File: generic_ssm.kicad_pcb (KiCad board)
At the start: 4 copper layers, 80 x 80 mm, 20 parts, among them J1 RST_JMP, J2 DEBUG CONN, J3 PROGRAMMING PORT, SW1 SW_RST, U1 SN65HVD233, U2 ATMEGA32M1-MU, Y1 8MHz

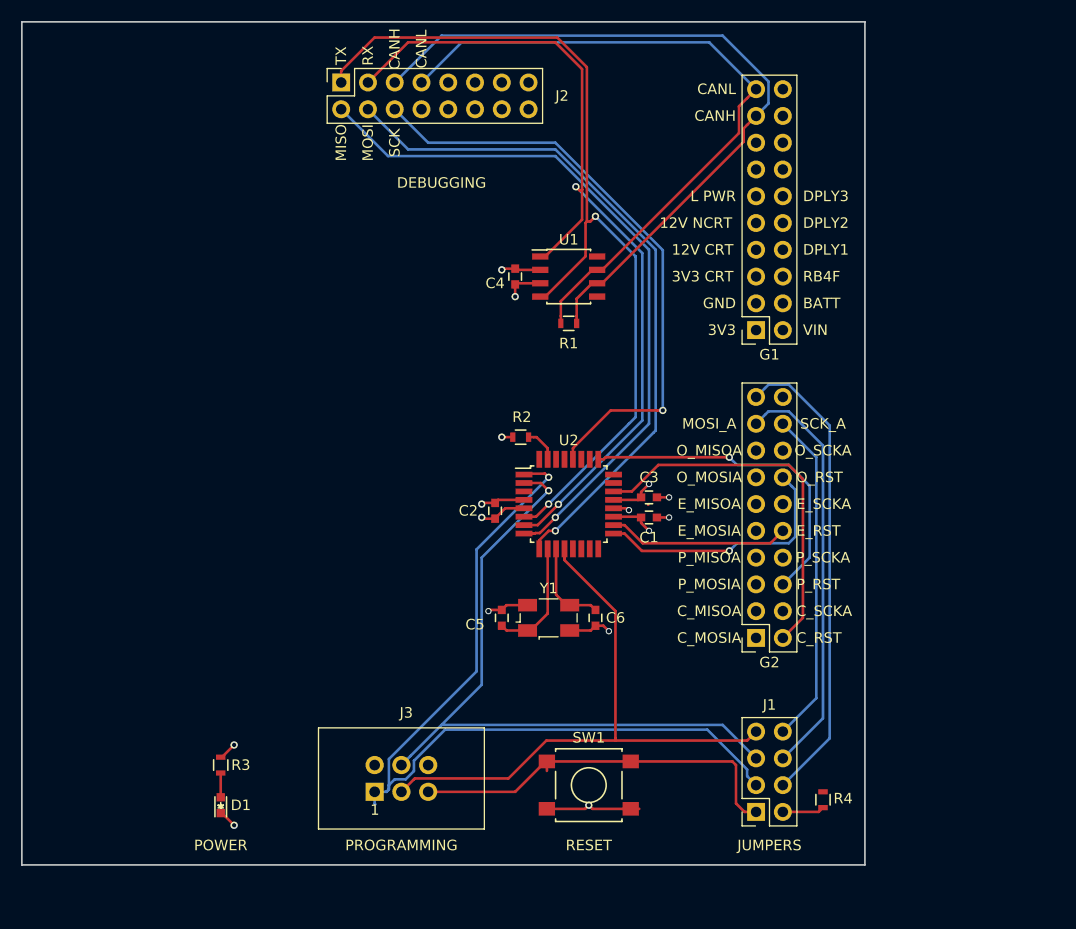
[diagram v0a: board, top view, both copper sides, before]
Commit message: Ease-of-use changes to PCB routing.
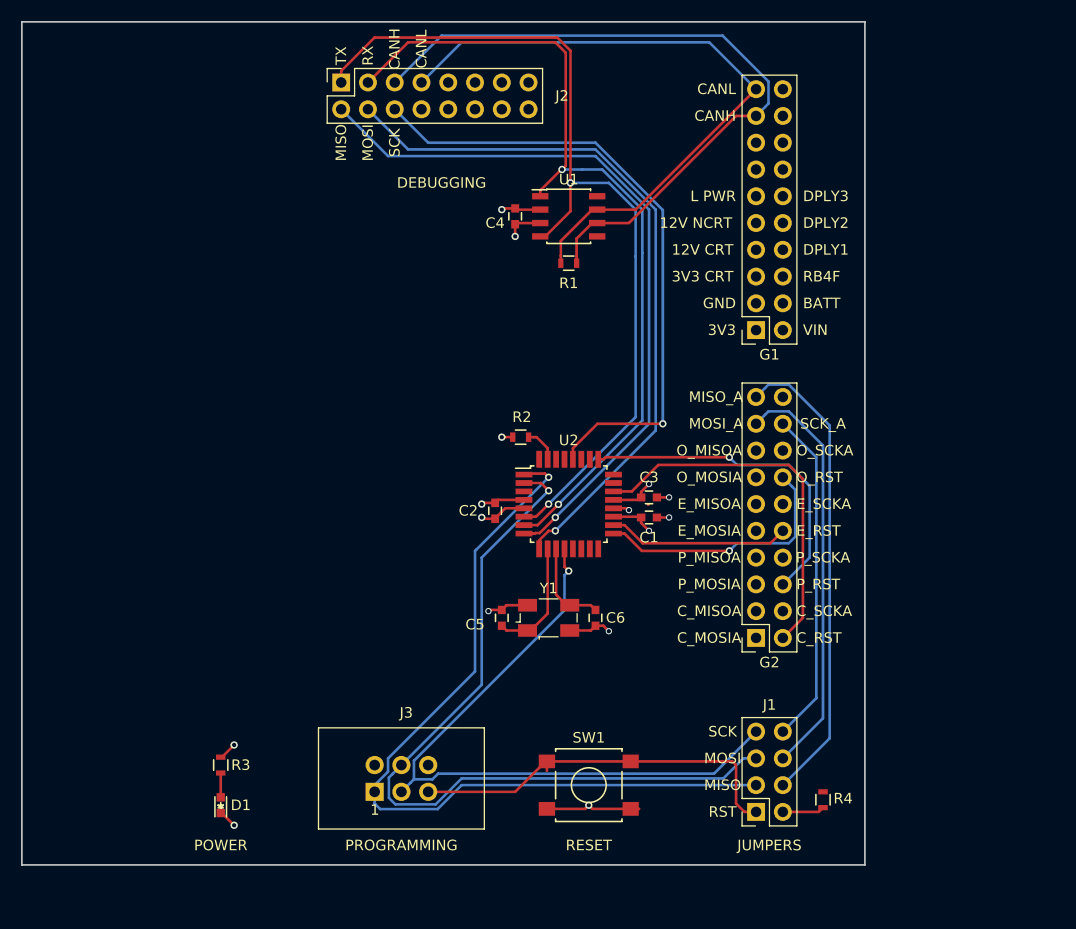
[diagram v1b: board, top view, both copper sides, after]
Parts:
- moved C4 5.72 mm to (146.8, 68.5)
- moved R1 5.72 mm to (151.9, 72.9)
- moved U1 5.72 mm to (151.9, 68.5)
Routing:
- net /MOSI_A: track 65.8 -> 75.1 mm
- net /SCK_A: track 57.3 -> 64.1 mm, vias 0 -> 1
- net /MISO_A: track 81.7 -> 77.8 mm
- net /CANL: track 65.6 -> 62.2 mm
- net /RX_CAN: track 83.6 -> 80.4 mm
- net /SCK: track 57.3 -> 60.2 mm
- net /CANH: track 70.2 -> 67.5 mm
- net /MOSI: track 66.2 -> 68.4 mm
- net /MISO: track 68.2 -> 70.5 mm
- net /TX_CAN: track 86.9 -> 85.2 mm
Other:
- board text added: "MISO_A"
- board text added: "RST"

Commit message: Minor Changes
Fixed via sizes, fixed resistors on schematic
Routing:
- net /SCK: track 60.2 -> 61.2 mm
- net GND: track 30.9 -> 31.5 mm
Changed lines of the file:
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@@
     (links 64)
     (no_connects 19)
-    (area 99.924999 49.924999 180.075001 130.075001)
+    (area 99.924999 46.723 218.11224 130.075001)
     (thickness 1.6)
     (drawings 56)
-    (tracks 271)
+    (tracks 280)
     (zones 0)
     (modules 20)
@@
     (aux_axis_origin 0 0)
     (grid_origin 12.192 12.573)
-    (visible_elements FFFEFF7F)
+    (visible_elements 7FFFFFFF)
     (pcbplotparams
       (layerselection 0x00030_80000001)
@@
   (gr_line (start 100 50) (end 180 50) (angle 90) (layer Edge.Cuts) (width 0.15))
   (segment (start 159.422001 95.823001) (end 159.487001 95.758001) (width 0.25) (layer F.Cu) (net 0))
+  (segment (start 157.5862 96.3122) (end 157.7894 96.3122) (width 0.25) (layer F.Cu) (net 1))
+  (via (at 157.861 96.2406) (size 0.7) (drill 0.4) (layers F.Cu B.Cu) (net 1))
+  (segment (start 157.7894 96.3122) (end 157.861 96.2406) (width 0.25) (layer F.Cu) (net 1))
+  (via (at 155.702 107.823) (size 0.7) (drill 0.4) (layers F.Cu B.Cu) (net 1))
+  (segment (start 144.272 105.918) (end 144.387 105.803) (width 0.25) (layer F.Cu) (net 1))
+  (segment (start 144.387 105.803) (end 144.272 105.918) (width 0.25) (layer F.Cu) (net 1))
+  (via (at 144.387 105.803) (size 0.7) (drill 0.4) (layers F.Cu B.Cu) (net 1))
+  (segment (start 144.387 105.803) (end 144.3736 105.8164) (width 0.25) (layer B.Cu) (net 1))
+  (segment (start 144.3736 105.8164) (end 144.3228 105.8164) (width 0.25) (layer B.Cu) (net 1))
   (segment (start 149.822 124.678) (end 153.452 124.678) (width 0.25) (layer F.Cu) (net 1))
   (segment (start 153.452 124.678) (end 153.797 124.333) (width 0.25) (layer F.Cu) (net 1))
@@
   (segment (start 157.772 124.678) (end 158.587 124.678) (width 0.25) (layer F.Cu) (net 1))
   (segment (start 156.142 96.158) (end 157.432 96.158) (width 0.25) (layer F.Cu) (net 1))
-  (via (at 157.607 96.333) (size 0.6) (drill 0.4) (layers F.Cu B.Cu) (net 1))
-  (segment (start 157.432 96.158) (end 157.607 96.333) (width 0.25) (layer F.Cu) (net 1))
+  (segment (start 157.432 96.158) (end 157.5862 96.3122) (width 0.25) (layer F.Cu) (net 1))
+  (segment (start 157.5862 96.3122) (end 157.607 96.333) (width 0.25) (layer F.Cu) (net 1))
   (segment (start 160.262 97.028) (end 161.417 97.028) (width 0.25) (layer F.Cu) (net 1))
-  (via (at 161.417 97.028) (size 0.6) (drill 0.4) (layers F.Cu B.Cu) (net 1))
+  (via (at 161.417 97.028) (size 0.7) (drill 0.4) (layers F.Cu B.Cu) (net 1))
   (segment (start 160.262 95.123) (end 161.417 95.123) (width 0.25) (layer F.Cu) (net 1))
-  (via (at 161.417 95.123) (size 0.6) (drill 0.4) (layers F.Cu B.Cu) (net 1))
+  (via (at 161.417 95.123) (size 0.7) (drill 0.4) (layers F.Cu B.Cu) (net 1))
   (segment (start 145.542 105.803) (end 144.387 105.803) (width 0.25) (layer F.Cu) (net 1))
-  (segment (start 144.387 105.803) (end 144.272 105.918) (width 0.25) (layer F.Cu) (net 1))
-  (via (at 144.272 105.918) (size 0.6) (drill 0.4) (layers F.Cu B.Cu) (net 1))
   (segment (start 147.987 105.353) (end 145.992 105.353) (width 0.25) (layer F.Cu) (net 1))
   (segment (start 145.992 105.353) (end 145.542 105.803) (width 0.25) (layer F.Cu) (net 1))
   (segment (start 154.432 107.303) (end 155.182 107.303) (width 0.25) (layer F.Cu) (net 1))
   (segment (start 155.182 107.303) (end 155.702 107.823) (width 0.25) (layer F.Cu) (net 1))
-  (via (at 155.702 107.823) (size 0.6) (drill 0.4) (layers F.Cu B.Cu) (net 1))
   (segment (start 151.987 107.753) (end 153.982 107.753) (width 0.25) (layer F.Cu) (net 1))
   (segment (start 153.982 107.753) (end 154.432 107.303) (width 0.25) (layer F.Cu) (net 1))
+  (segment (start 159.4993 93.8657) (end 159.8041 93.8657) (width 0.25) (layer F.Cu) (net 2))
+  (via (at 159.893 93.7768) (size 0.7) (drill 0.4) (layers F.Cu B.Cu) (net 2))
+  (segment (start 159.8041 93.8657) (end 159.893 93.7768) (width 0.25) (layer F.Cu) (net 2))
   (segment (start 146.582 89.408) (end 145.542 89.408) (width 0.25) (layer F.Cu) (net 2))
   (via (at 145.542 89.408) (size 0.7) (drill 0.4) (layers F.Cu B.Cu) (net 2))
@@
   (via (at 120.142 118.618) (size 0.7) (drill 0.4) (layers F.Cu B.Cu) (net 2))
   (segment (start 158.762 95.123) (end 158.762 94.603) (width 0.25) (layer F.Cu) (net 2))
-  (segment (start 158.762 94.603) (end 159.512 93.853) (width 0.25) (layer F.Cu) (net 2))
-  (via (at 159.512 93.853) (size 0.6) (drill 0.4) (layers F.Cu B.Cu) (net 2))
+  (segment (start 158.762 94.603) (end 159.4993 93.8657) (width 0.25) (layer F.Cu) (net 2))
+  (segment (start 159.4993 93.8657) (end 159.512 93.853) (width 0.25) (layer F.Cu) (net 2))
   (segment (start 156.142 95.358) (end 158.527 95.358) (width 0.25) (layer F.Cu) (net 2))
   (segment (start 158.527 95.358) (end 158.762 95.123) (width 0.25) (layer F.Cu) (net 2))
   (segment (start 158.762 97.028) (end 158.762 97.548) (width 0.25) (layer F.Cu) (net 2))
   (segment (start 158.762 97.548) (end 159.512 98.298) (width 0.25) (layer F.Cu) (net 2))
-  (via (at 159.512 98.298) (size 0.6) (drill 0.4) (layers F.Cu B.Cu) (net 2))
+  (via (at 159.512 98.298) (size 0.7) (drill 0.4) (layers F.Cu B.Cu) (net 2))
   (segment (start 156.142 96.958) (end 158.692 96.958) (width 0.25) (layer F.Cu) (net 2))
   (segment (start 158.692 96.958) (end 158.762 97.028) (width 0.25) (layer F.Cu) (net 2))
@@
   (segment (start 149.9926 98.298) (end 150.622 98.298) (width 0.25) (layer F.Cu) (net 49))
   (via (at 150.622 98.298) (size 0.7) (drill 0.4) (layers F.Cu B.Cu) (net 49))
-  (segment (start 160.822 88.138) (end 160.822 67.85518) (width 0.25) (layer B.Cu) (net 50))
-  (segment (start 160.822 67.85518) (end 154.43482 61.468) (width 0.25) (layer B.Cu) (net 50))
+  (segment (start 161.3916 88.138) (end 161.4424 67.8688) (width 0.25) (layer B.Cu) (net 50))
+  (segment (start 161.4424 67.8688) (end 154.43482 61.468) (width 0.25) (layer B.Cu) (net 50))
   (segment (start 154.43482 61.468) (end 138.557 61.468) (width 0.25) (layer B.Cu) (net 50))
   (segment (start 138.557 61.468) (end 135.382 58.293) (width 0.25) (layer B.Cu) (net 50))
   (segment (start 152.292 91.508) (end 152.292 90.458) (width 0.25) (layer F.Cu) (net 50))
   (segment (start 152.292 90.458) (end 154.612 88.138) (width 0.25) (layer F.Cu) (net 50))
-  (segment (start 154.612 88.138) (end 160.822 88.138) (width 0.25) (layer F.Cu) (net 50))
-  (via (at 160.822 88.138) (size 0.7) (drill 0.4) (layers F.Cu B.Cu) (net 50))
+  (segment (start 154.612 88.138) (end 161.3916 88.138) (width 0.25) (layer F.Cu) (net 50))
+  (via (at 161.3916 88.138) (size 0.7) (drill 0.4) (layers F.Cu B.Cu) (net 50))
   (segment (start 154.592 69.088) (end 157.60841 69.088) (width 0.25) (layer F.Cu) (net 60))
   (segment (start 157.60841 69.088) (end 167.76841 58.928) (width 0.25) (layer F.Cu) (net 60))

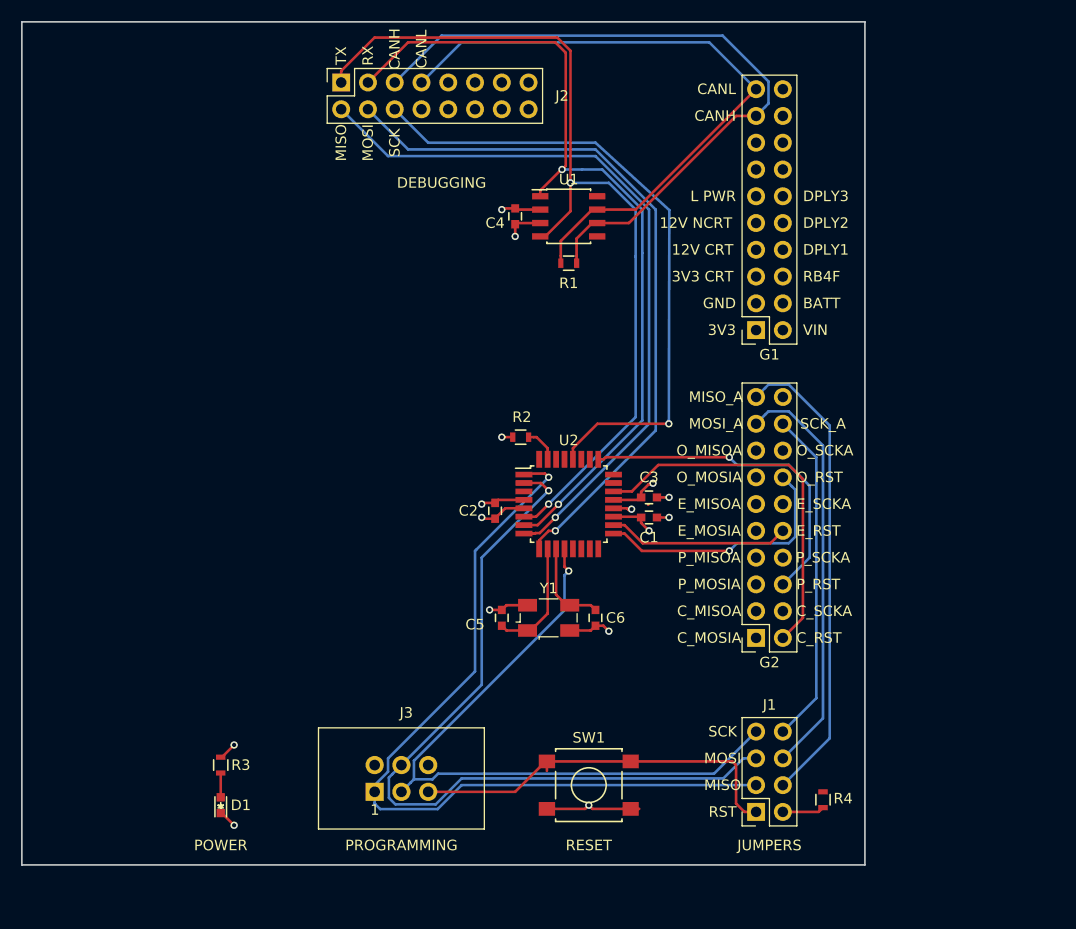
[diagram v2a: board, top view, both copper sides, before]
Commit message: Remade PCB layout for different header positions.
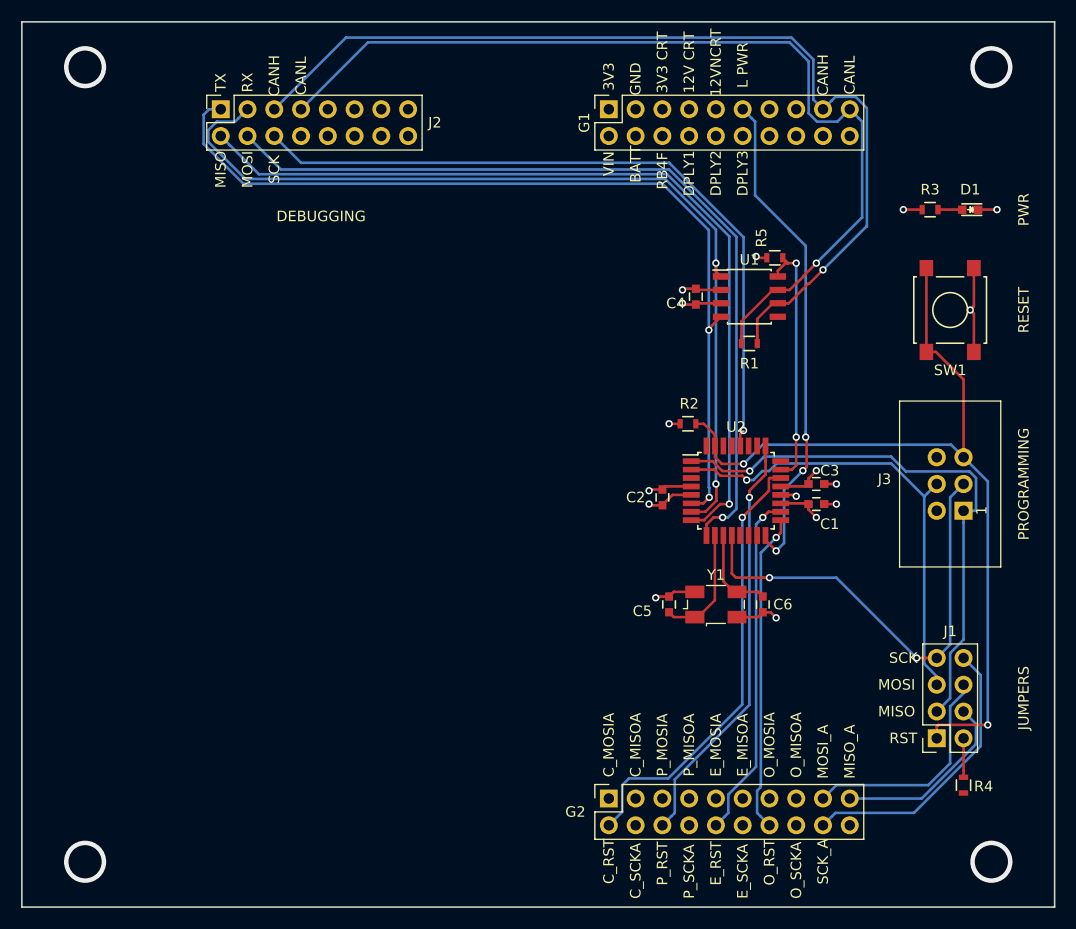
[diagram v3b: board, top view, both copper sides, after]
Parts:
- added R5: 1K, Resistors_SMD:R_0603, F.Cu at (171.4, 72.4)
- R2: value 120R -> 10K
- R4: value 10R -> 120R
- U1: value SN65HVD233 -> SN65HVD230
- moved D1 90.8 mm to (190.0, 67.8), turned to 180 degrees
- moved R3 85.5 mm to (186.2, 67.8), turned to 0 degrees
- moved J3 61.9 mm to (189.4, 96.4), turned to 90 degrees
- moved SW1 56.6 mm to (188.1, 77.3), turned to 90 degrees
- moved G1 25.2 mm to (155.7, 58.3), turned to 90 degrees
- moved G2 20.7 mm to (155.7, 123.7), turned to 90 degrees
- moved R1 18.8 mm to (169.0, 80.5)
- moved U1 18.8 mm to (169.0, 76.1)
- moved C4 18.8 mm to (164.0, 76.1)
- moved J1 18.5 mm to (186.8, 118.0)
- moved C1 15.9 mm to (175.4, 95.8)
- moved C2 15.9 mm to (160.8, 95.1)
- moved C3 15.9 mm to (175.4, 93.9)
- moved C5 15.9 mm to (161.4, 105.3)
- moved C6 15.9 mm to (170.3, 105.3)
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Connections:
- U1 pad 8: GND -> /CAN_LPWR
- U2 pad 16: Net-(U2-Pad16) -> /LOPWR
- U2 pad 23: Net-(U2-Pad23) -> /CAN_LPWR
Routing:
- net /LOPWR: track 0.00 -> 48.0 mm, vias 0 -> 3
- net /RST: track 40.7 -> 81.7 mm, vias 0 -> 2
- net /MOSI_A: track 75.1 -> 44.5 mm
- net /CANL: track 62.2 -> 90.1 mm, vias 0 -> 1
- net /MISO_A_COMMON: track 45.0 -> 18.5 mm
- net /CANH: track 67.5 -> 93.1 mm, vias 0 -> 1
- net /MISO_A: track 77.8 -> 53.2 mm
- net /CAN_LPWR: track 0.00 -> 24.1 mm, vias 0 -> 2
- net /SCK_A: track 64.1 -> 43.9 mm, vias 1 -> 2
- net /MOSI_A_COMMON: track 39.4 -> 21.4 mm
- net /EPS_RST: track 17.3 -> 33.0 mm, vias 0 -> 1
- net /MOSI: track 68.4 -> 80.7 mm
- net /MISO: track 70.5 -> 81.9 mm
- net /PAY_RST: track 31.7 -> 40.1 mm
- net /SCK: track 61.2 -> 68.4 mm
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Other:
- board size 80 x 80 mm -> 98 x 84 mm
- board text added: "12VNCRT"
- board text added: "DON'T FORGET TO CONNECT R4"
- board text added: "PWR"
- board text added: "REMEMBER TO CONNECT YOUR SPI_A LINES TO THE JUMPERS ONCE YOU RENAME THEM. ALSO, DON'T FORGET TO REMOVE THE TRACE FOR XXX_RST CORRESPONDING TO YOUR BOARD THIS WILL CAUSE PROBLEMS IF YOU DON'T"
- board text removed: "12V NCRT"
- board text removed: "ALSO, DON'T FORGET TO REMOVE THE TRACE FOR XXX_RST CORRESPONDING TO YOUR BOARD THIS WILL CAUSE PROBLEMS IF YOU DON'T"
- board text removed: "DON'T FORGET TO CONNECT R4 & YOUR SPI LINES."
- board text removed: "POWER"
